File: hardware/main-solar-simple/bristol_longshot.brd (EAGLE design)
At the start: 14 x 64 mm, 66 parts, among them U1 SAM_D20E, U2 SI4060, U3 UBLOX_MAX, U4 SST25WF040BT-40I/NP, U5 TG-5006CJ, U6 LTC3105EDDPBF, U7 TPS3123, U8 SN74LVC1G32DCKR, U9 MS5607-02BA03

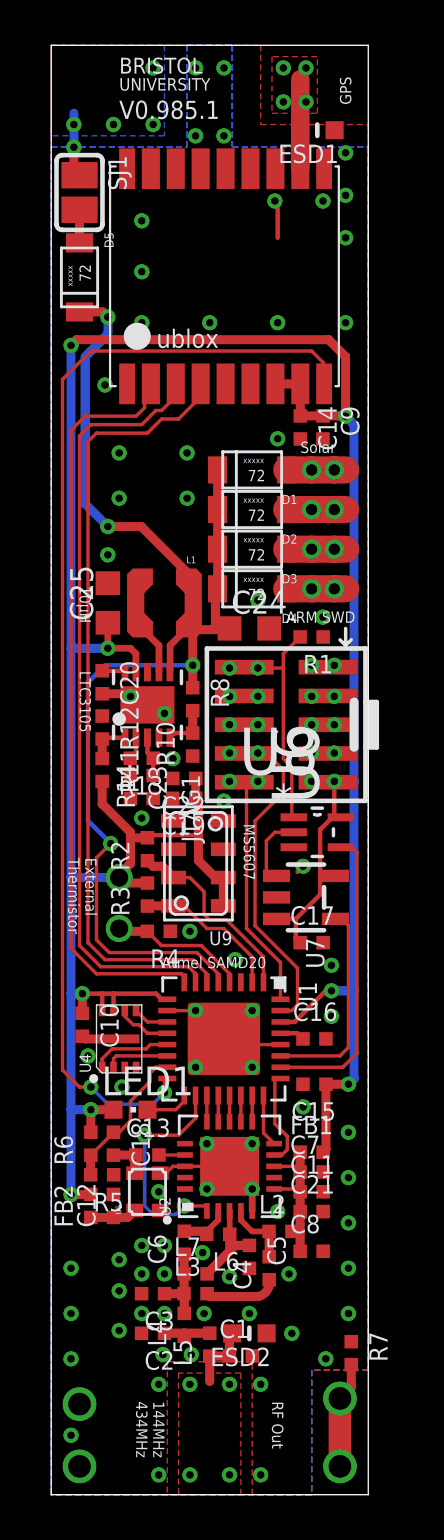
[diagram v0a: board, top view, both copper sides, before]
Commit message: Hardware v0.985.3, reduce external thermistor holes to 0.5mm dia
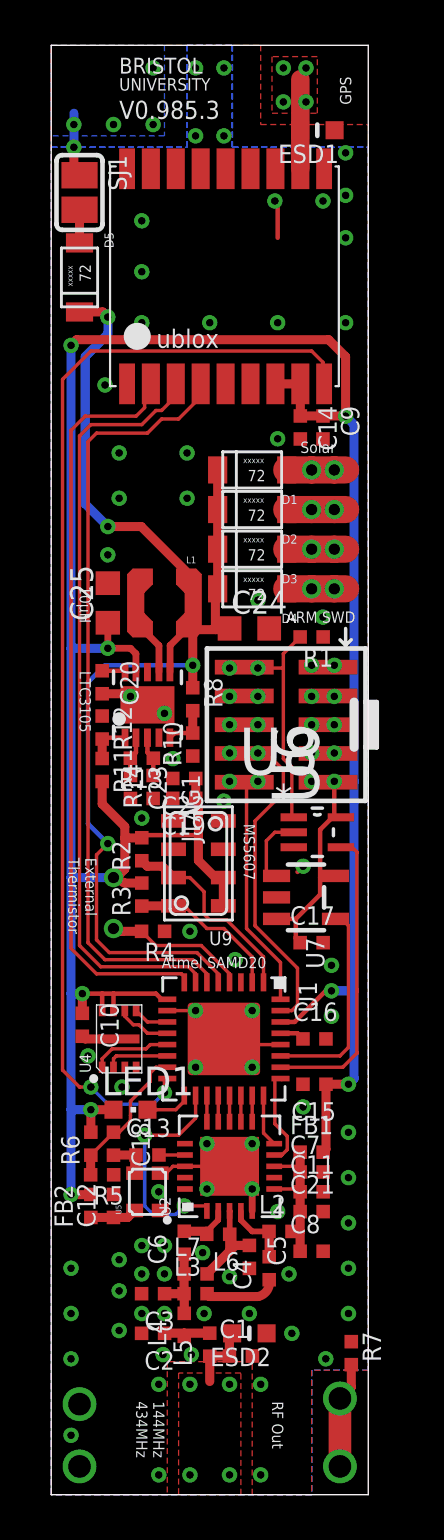
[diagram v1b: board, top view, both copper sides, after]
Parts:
- C1, C10, C11, C12, C13, C14, C15, C16, C17, C18, C19, C2, C20, C21, C22, C23, C3, C4, C5, C6, C7, C8, C9, FB1, FB2, L2, L3, L4, L5, L6, L7: device microbuilder_v3:_0402 -> microbuilder_v3:_0402@1
- moved R2 0.25 mm to (4.00, 28.5)
- moved R3 0.25 mm to (4.00, 26.5)
- moved R4 0.25 mm to (4.50, 24.9)
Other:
- board text added: "V0.985.3"
- board text removed: "V0.985.1"
